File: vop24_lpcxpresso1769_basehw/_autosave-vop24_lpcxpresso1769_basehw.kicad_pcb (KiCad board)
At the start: 2 copper layers, 113 parts, among them J1 Micro_SD_Card, J101 Conn_01x03_Male, J201 Screw_Terminal_01x02, J301 USB_B_Micro, J302 Conn_01x06_Male, J303 Conn_01x05_Male, J304 Screw_Terminal_01x02, J401 Conn_01x02, J402 Conn_01x02, J403 Conn_01x02, J404 Conn_01x04, J405 Conn_01x04, J406 Conn_01x04, U1 LPCXpresso1769, U101 MCP1700T-3302E_TT, U102 MCP1700T-3302E_TT, U103 TPS63001, U201 LM358, U301 TPD4S014, U302 LTC4411, U303 LT1512, U401 ADS1292, U402 LM334, U403 LM334, U404 LM334

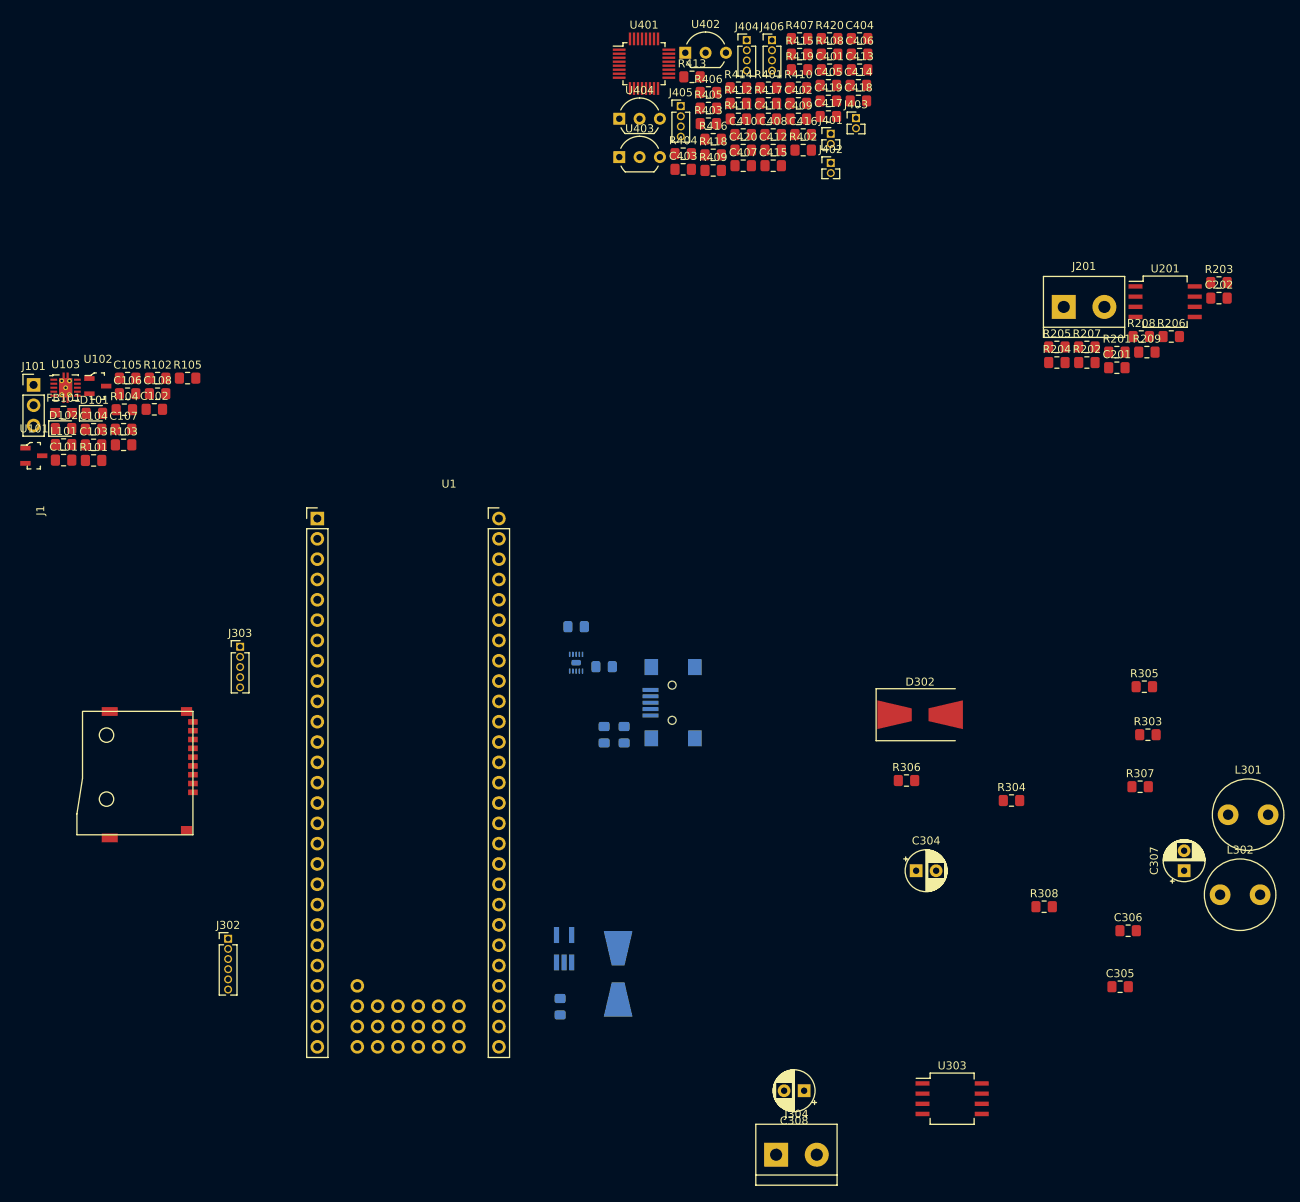
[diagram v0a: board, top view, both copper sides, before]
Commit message: Primer commit sobre el diseño del PCB. Se agruparon algunas hojas de esquemáticos. No se empezó a rutear
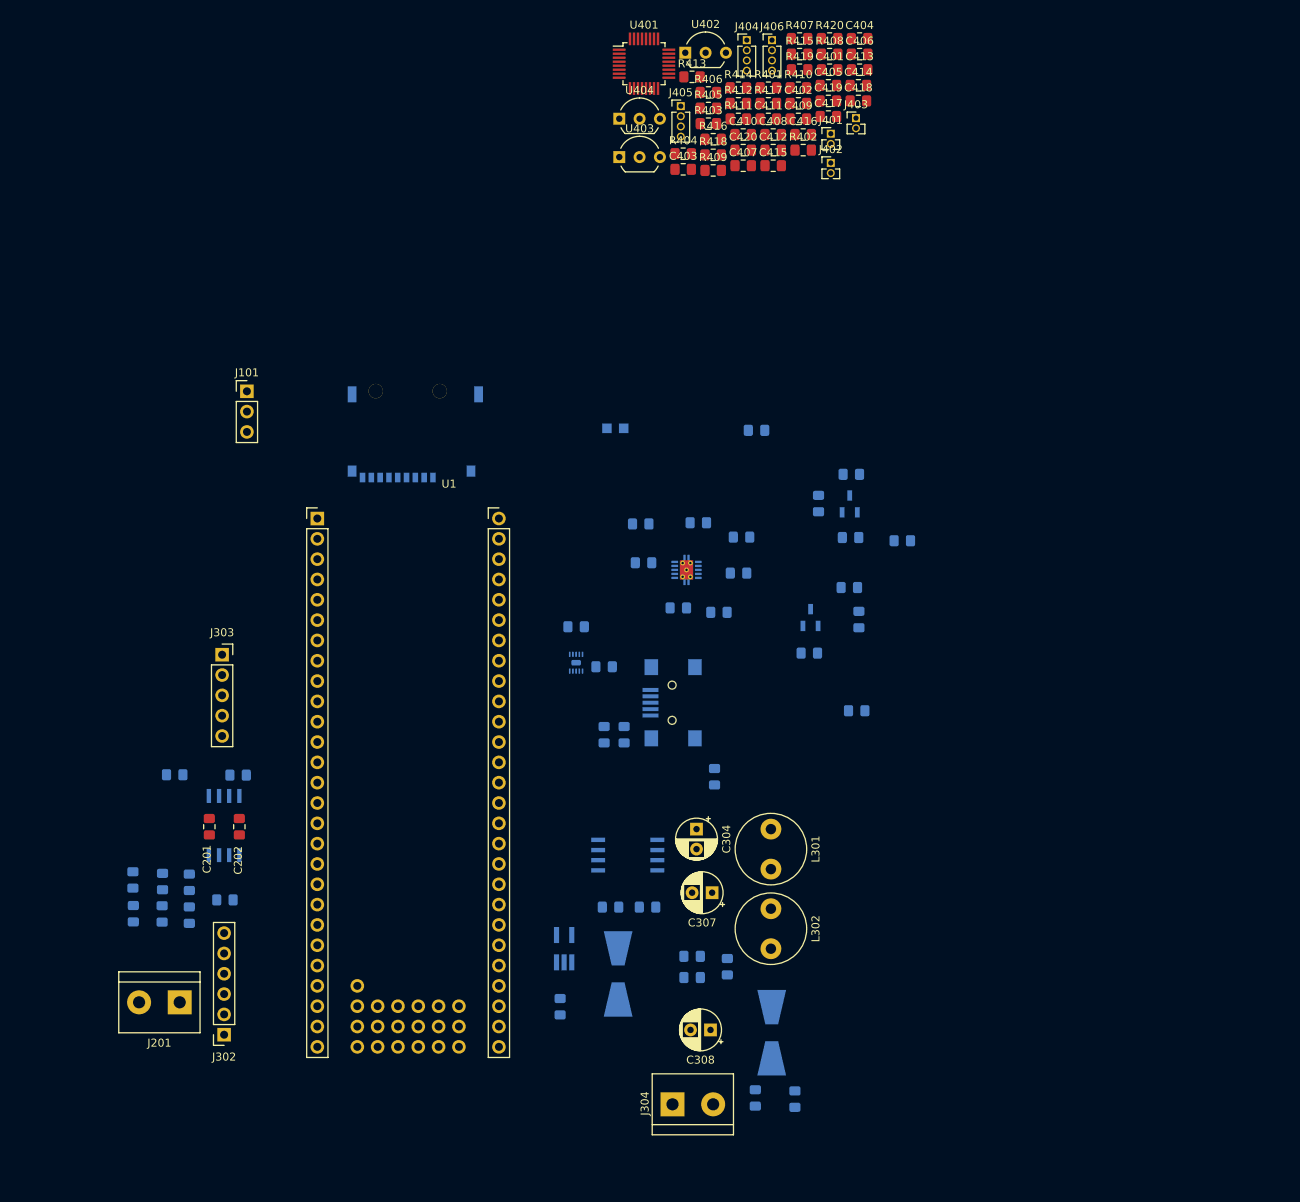
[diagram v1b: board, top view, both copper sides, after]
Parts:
- C101, C102, C103, C104, C105, C106, C107, C108, C305, C306, D101, D102, D302, FB101, J1, L101, R101, R102, R103, R104, R105, R201, R202, R203, R204, R205, R206, R207, R208, R209, R303, R304, R305, R306, R307, R308, U101, U102, U103, U201, U303: moved to B.Cu
- J302: footprint Connector_PinHeader_1.27mm:PinHeader_1x06_P1.27mm_Vertical -> Connector_PinSocket_2.54mm:PinSocket_1x06_P2.54mm_Vertical
- J303: footprint Connector_PinHeader_1.27mm:PinHeader_1x05_P1.27mm_Vertical -> Connector_PinSocket_2.54mm:PinSocket_1x05_P2.54mm_Vertical
- moved R203 144.3 mm to (61.8, 137.5)
- moved R206 143.3 mm to (60.3, 150.8), turned to 270 degrees
- moved J201 140.6 mm to (62.5, 165.9), turned to 180 degrees
- moved R201 139.6 mm to (56.6, 150.7), turned to 90 degrees
- moved R208 139.3 mm to (63.6, 155.1), turned to 90 degrees
- moved C202 139.1 mm to (69.9, 144.0), turned to 90 degrees
- moved R209 136.8 mm to (63.6, 150.9), turned to 270 degrees
- moved U201 134.6 mm to (68.0, 143.8), turned to 270 degrees
- moved R204 134.4 mm to (56.6, 154.9), turned to 90 degrees
- moved R205 132.4 mm to (60.2, 154.9), turned to 270 degrees
- moved R207 128.0 mm to (68.1, 153.2), turned to 180 degrees
- moved C201 127.1 mm to (66.2, 144.0), turned to 90 degrees
- moved R202 118.0 mm to (69.8, 137.6)
- moved D102 105.8 mm to (152.8, 108.2)
- moved U101 102.2 mm to (146.2, 103.7), turned to 90 degrees
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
